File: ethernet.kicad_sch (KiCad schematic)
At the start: 58 parts, among them J8001 Bus_RJ45_5-2337992-8, U8001 KSZ9031RNXCA, Y8001 Oscillator_SMD_25MHz_KX-7

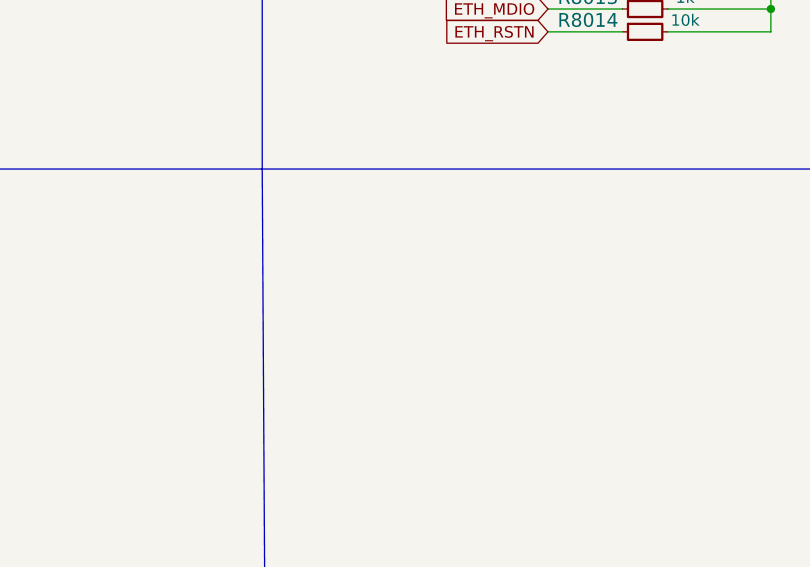
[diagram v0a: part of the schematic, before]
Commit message: Improve PCB after layout review
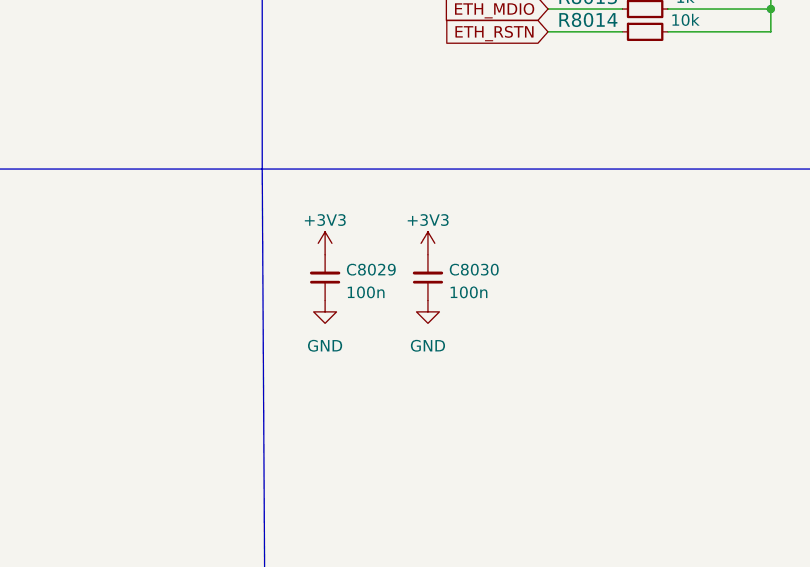
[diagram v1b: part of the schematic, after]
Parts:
- added C8029, C8030: C_100n_0402, antmicro-footprints:C_0402_1005Metric, symbol antmicroCapacitors0402:C_100n_0402
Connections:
- net +3V3: now also C8029.2, C8030.2
- net GND: now also C8029.1, C8030.1
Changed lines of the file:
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@@
     (pin "2")
+  )
+  (symbol (lib_id "sodimm-ddr5-tester:GND") (at 147.32 189.865 0) (unit 1)
+    (in_bom yes) (on_board yes) (fields_autoplaced)
+    (property "Reference" "#PWR0303" (id 0) (at 147.32 196.215 0)
+      (effects (font (size 1.27 1.27)) hide)
+    )
+    (property "Value" "GND" (id 1) (at 147.32 194.945 0))
+    (property "Footprint" "" (id 2) (at 147.32 189.865 0)
+      (effects (font (size 1.27 1.27)) hide)
+    )
+    (property "Datasheet" "" (id 3) (at 147.32 189.865 0)
+      (effects (font (size 1.27 1.27)) hide)
+    )
+    (property "Author" "Antmicro" (id 4) (at 156.21 197.485 0)
+      (effects (font (size 1.27 1.27) (thickness 0.15)) (justify left bottom) hide)
+    )
+    (property "License" "Apache-2.0" (id 5) (at 156.21 200.025 0)
+      (effects (font (size 1.27 1.27) (thickness 0.15)) (justify left bottom) hide)
+    )
+    (pin "1")
+  )
+  (symbol (lib_id "sodimm-ddr5-tester:+3V3") (at 158.75 184.785 0) (unit 1)
+    (in_bom yes) (on_board yes)
+    (property "Reference" "#PWR0305" (id 0) (at 158.75 188.595 0)
+      (effects (font (size 1.27 1.27)) hide)
+    )
+    (property "Value" "+3V3" (id 1) (at 158.75 180.975 0))
+    (property "Footprint" "" (id 2) (at 158.75 184.785 0)
+      (effects (font (size 1.27 1.27)) hide)
+    )
+    (property "Datasheet" "" (id 3) (at 158.75 184.785 0)
+      (effects (font (size 1.27 1.27)) hide)
+    )
+    (pin "1")
   )
   (symbol (lib_id "sodimm-ddr5-tester:GNDS") (at 78.74 244.475 0) (mirror y) (unit 1)
@@
     (pin "1")
   )
+  (symbol (lib_id "antmicroCapacitors0402:C_100n_0402") (at 158.75 189.865 90) (unit 1)
+    (in_bom yes) (on_board yes) (fields_autoplaced)
+    (property "Reference" "C8030" (id 0) (at 161.0741 186.488 90)
+      (effects (font (size 1.27 1.27) (thickness 0.15)) (justify right))
+    )
+    (property "Value" "C_100n_0402" (id 1) (at 168.91 169.545 0)
+      (effects (font (size 1.27 1.27) (thickness 0.15)) (justify left bottom) hide)
+    )
+    (property "Footprint" "antmicro-footprints:C_0402_1005Metric" (id 2) (at 171.45 169.545 0)
+      (effects (font (size 1.27 1.27) (thickness 0.15)) (justify left bottom) hide)
+    )
+    (property "Datasheet" "https://www.murata.com/products/productdetail?partno=GRM155R61H104KE14%23" (id 3) (at 173.99 169.545 0)
+      (effects (font (size 1.27 1.27) (thickness 0.15)) (justify left bottom) hide)
+    )
+    (property "MPN" "GRM155R61H104KE14D" (id 4) (at 176.53 169.545 0)
+      (effects (font (size 1.27 1.27) (thickness 0.15)) (justify left bottom) hide)
+    )
+    (property "Manufacturer" "Murata" (id 5) (at 179.07 169.545 0)
+      (effects (font (size 1.27 1.27) (thickness 0.15)) (justify left bottom) hide)
+    )
+    (property "License" "Apache-2.0" (id 6) (at 181.61 169.545 0)
+      (effects (font (size 1.27 1.27) (thickness 0.15)) (justify left bottom) hide)
+    )
+    (property "Author" "Antmicro" (id 7) (at 184.15 169.545 0)
+      (effects (font (size 1.27 1.27) (thickness 0.15)) (justify left bottom) hide)
+    )
+    (property "Val" "100n" (id 8) (at 161.0741 189.0117 90)
+      (effects (font (size 1.27 1.27) (thickness 0.15)) (justify right))
+    )
+    (property "Voltage" "50V" (id 9) (at 186.69 169.545 0)
+      (effects (font (size 1.27 1.27)) (justify left bottom) hide)
+    )
+    (property "Dielectric" "X5R" (id 10) (at 189.23 169.545 0)
+      (effects (font (size 1.27 1.27)) (justify left bottom) hide)
+    )
+    (pin "1")
+    (pin "2")
+  )
   (symbol (lib_id "antmicroFerriteBeadsandChips:FB_120Z_2A_Murata-BLM18PG_0603") (at 26.035 140.97 0) (unit 1)
     (in_bom yes) (on_board yes) (fields_autoplaced)
@@
     (pin "2")
   )
+  (symbol (lib_id "sodimm-ddr5-tester:+3V3") (at 147.32 184.785 0) (unit 1)
+    (in_bom yes) (on_board yes)
+    (property "Reference" "#PWR0302" (id 0) (at 147.32 188.595 0)
+      (effects (font (size 1.27 1.27)) hide)
+    )
+    (property "Value" "+3V3" (id 1) (at 147.32 180.975 0))
+    (property "Footprint" "" (id 2) (at 147.32 184.785 0)
+      (effects (font (size 1.27 1.27)) hide)
+    )
+    (property "Datasheet" "" (id 3) (at 147.32 184.785 0)
+      (effects (font (size 1.27 1.27)) hide)
+    )
+    (pin "1")
+  )
   (symbol (lib_id "sodimm-ddr5-tester:R_10k_0402") (at 180.34 147.32 0) (unit 1)
     (in_bom yes) (on_board yes)
@@
     (pin "1")
     (pin "2")
+  )
+  (symbol (lib_id "sodimm-ddr5-tester:GND") (at 158.75 189.865 0) (unit 1)
+    (in_bom yes) (on_board yes) (fields_autoplaced)
+    (property "Reference" "#PWR0304" (id 0) (at 158.75 196.215 0)
+      (effects (font (size 1.27 1.27)) hide)
+    )
+    (property "Value" "GND" (id 1) (at 158.75 194.945 0))
+    (property "Footprint" "" (id 2) (at 158.75 189.865 0)
+      (effects (font (size 1.27 1.27)) hide)
+    )
+    (property "Datasheet" "" (id 3) (at 158.75 189.865 0)
+      (effects (font (size 1.27 1.27)) hide)
+    )
+    (property "Author" "Antmicro" (id 4) (at 167.64 197.485 0)
+      (effects (font (size 1.27 1.27) (thickness 0.15)) (justify left bottom) hide)
+    )
+    (property "License" "Apache-2.0" (id 5) (at 167.64 200.025 0)
+      (effects (font (size 1.27 1.27) (thickness 0.15)) (justify left bottom) hide)
+    )
+    (pin "1")
   )
   (symbol (lib_id "sodimm-ddr5-tester:R_10k_0402") (at 180.34 152.4 0) (unit 1)
@@
     (pin "9")
   )
+  (symbol (lib_id "antmicroCapacitors0402:C_100n_0402") (at 147.32 189.865 90) (unit 1)
+    (in_bom yes) (on_board yes) (fields_autoplaced)
+    (property "Reference" "C8029" (id 0) (at 149.6441 186.488 90)
+      (effects (font (size 1.27 1.27) (thickness 0.15)) (justify right))
+    )
+    (property "Value" "C_100n_0402" (id 1) (at 157.48 169.545 0)
+      (effects (font (size 1.27 1.27) (thickness 0.15)) (justify left bottom) hide)
+    )
+    (property "Footprint" "antmicro-footprints:C_0402_1005Metric" (id 2) (at 160.02 169.545 0)
+      (effects (font (size 1.27 1.27) (thickness 0.15)) (justify left bottom) hide)
+    )
+    (property "Datasheet" "https://www.murata.com/products/productdetail?partno=GRM155R61H104KE14%23" (id 3) (at 162.56 169.545 0)
+      (effects (font (size 1.27 1.27) (thickness 0.15)) (justify left bottom) hide)
+    )
+    (property "MPN" "GRM155R61H104KE14D" (id 4) (at 165.1 169.545 0)
+      (effects (font (size 1.27 1.27) (thickness 0.15)) (justify left bottom) hide)
+    )
+    (property "Manufacturer" "Murata" (id 5) (at 167.64 169.545 0)
+      (effects (font (size 1.27 1.27) (thickness 0.15)) (justify left bottom) hide)
+    )
+    (property "License" "Apache-2.0" (id 6) (at 170.18 169.545 0)
+      (effects (font (size 1.27 1.27) (thickness 0.15)) (justify left bottom) hide)
+    )
+    (property "Author" "Antmicro" (id 7) (at 172.72 169.545 0)
+      (effects (font (size 1.27 1.27) (thickness 0.15)) (justify left bottom) hide)
+    )
+    (property "Val" "100n" (id 8) (at 149.6441 189.0117 90)
+      (effects (font (size 1.27 1.27) (thickness 0.15)) (justify right))
+    )
+    (property "Voltage" "50V" (id 9) (at 175.26 169.545 0)
+      (effects (font (size 1.27 1.27)) (justify left bottom) hide)
+    )
+    (property "Dielectric" "X5R" (id 10) (at 177.8 169.545 0)
+      (effects (font (size 1.27 1.27)) (justify left bottom) hide)
+    )
+    (pin "1")
+    (pin "2")
+  )
   (symbol (lib_id "sodimm-ddr5-tester:R_10k_0402") (at 180.34 149.86 0) (unit 1)

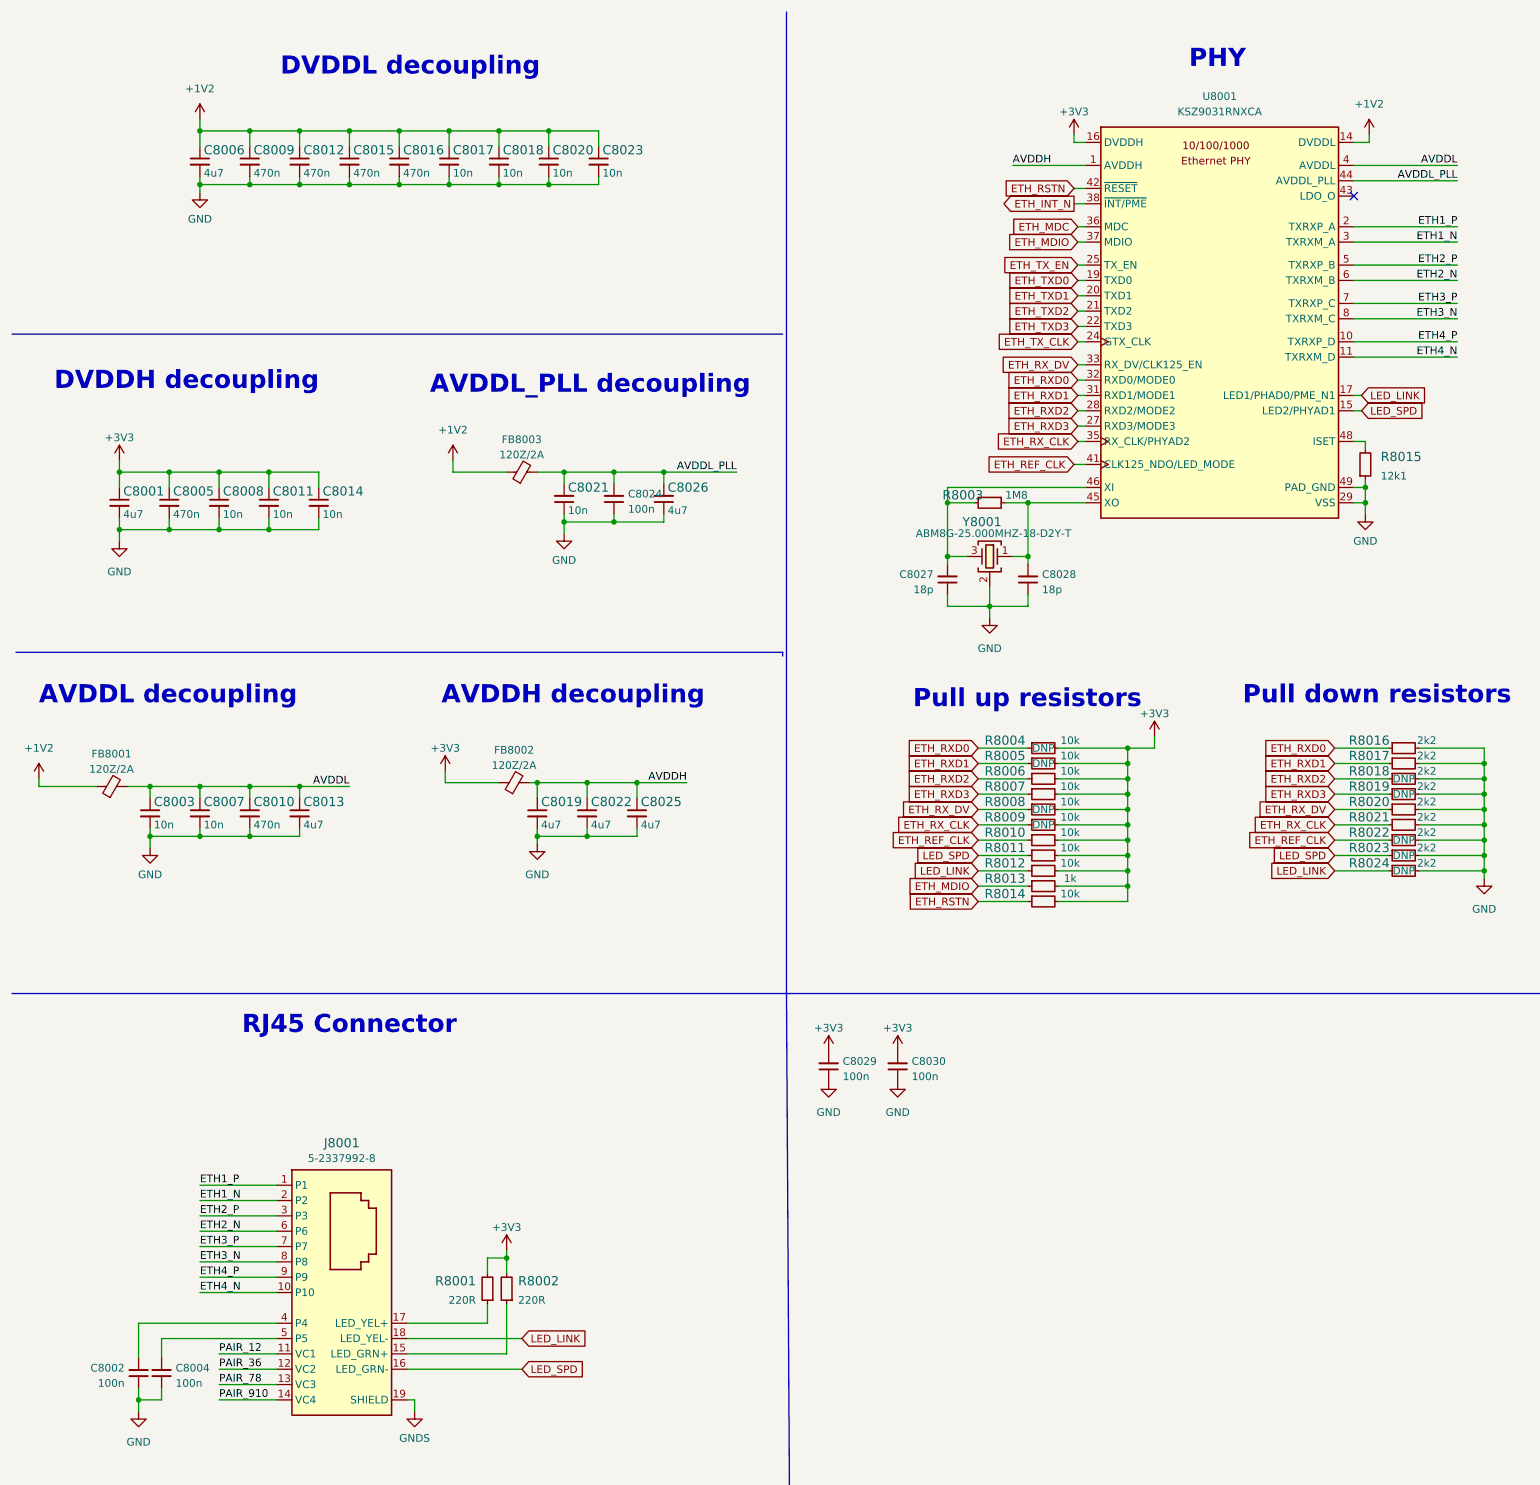
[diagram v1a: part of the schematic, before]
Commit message: Re-annotate schematic
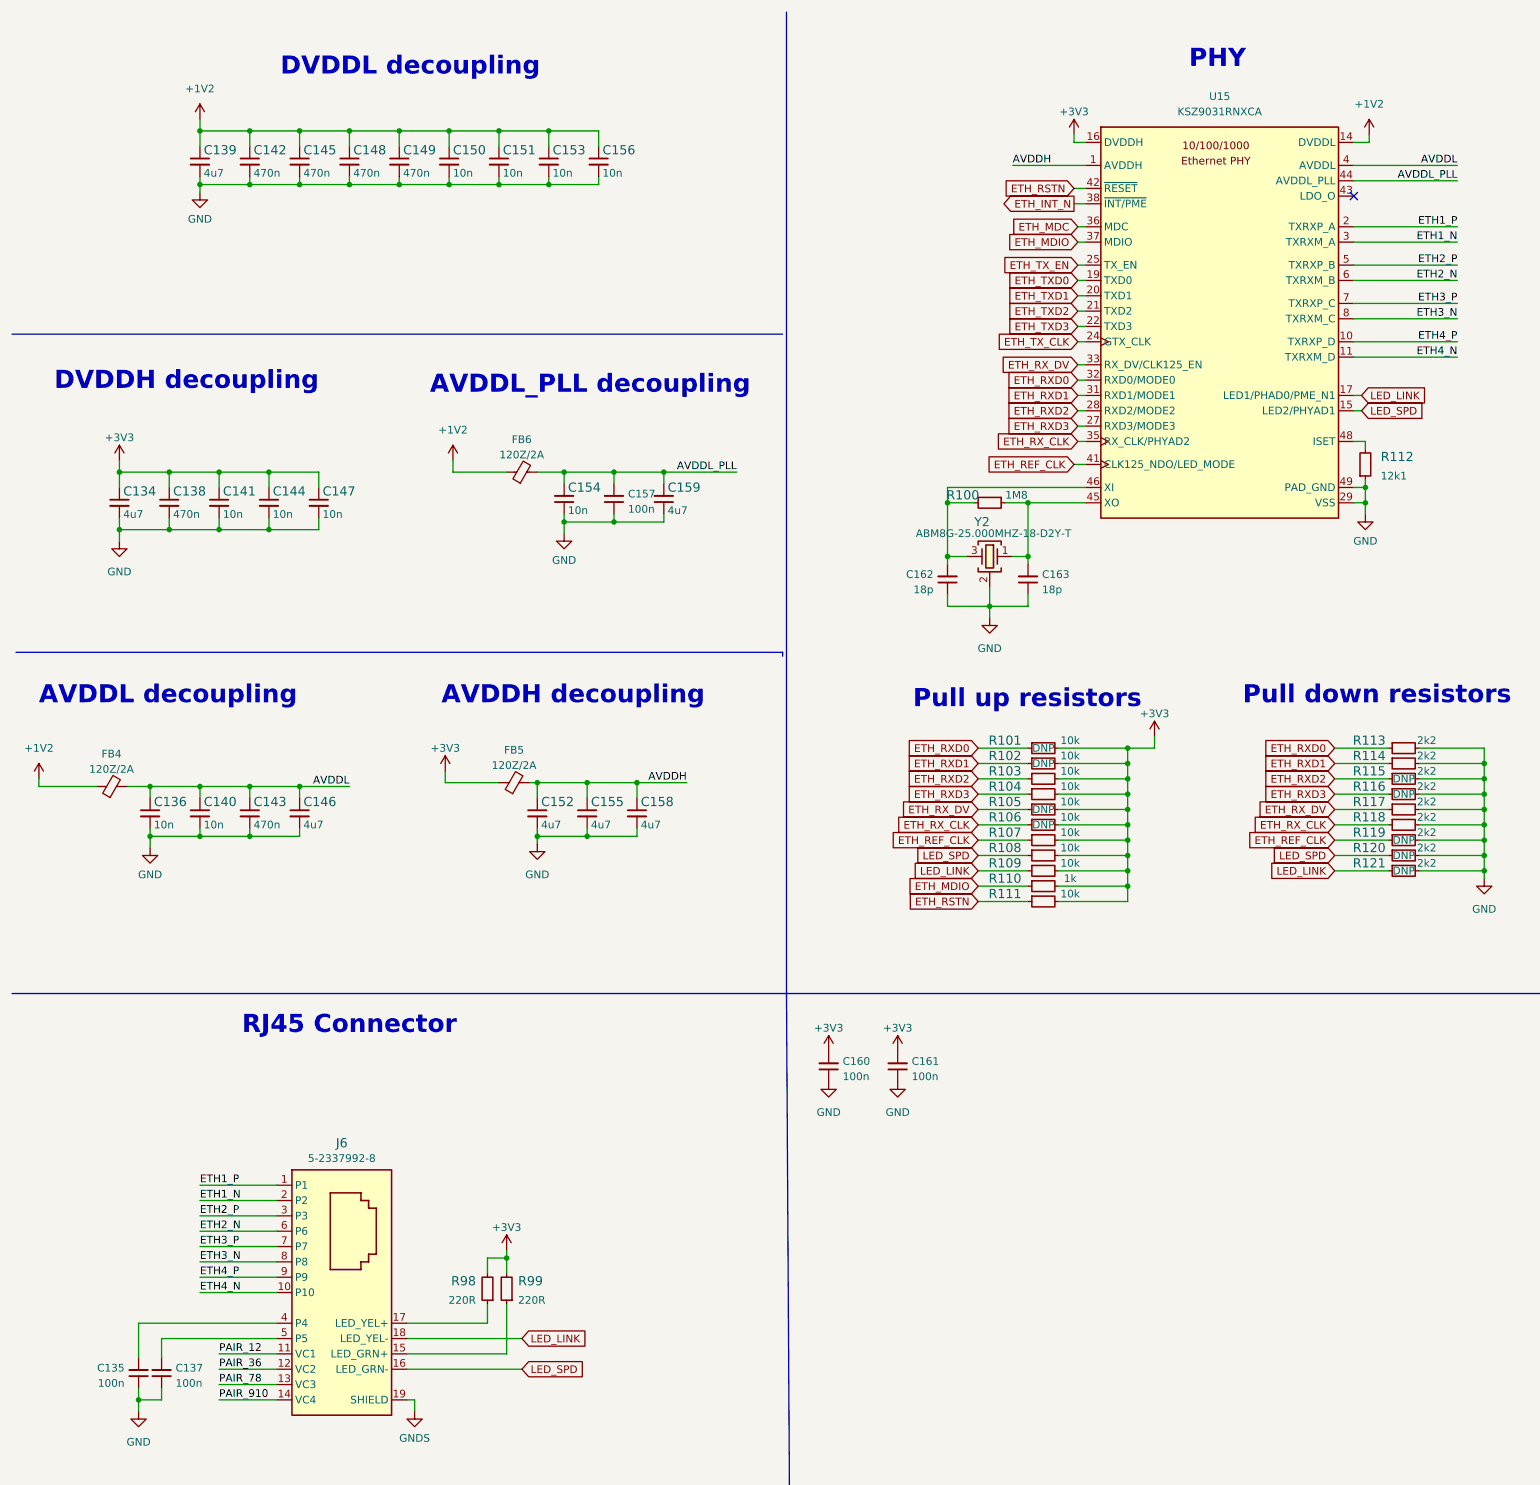
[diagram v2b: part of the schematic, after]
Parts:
- renumbered C8001 to C134, C8002 to C135, C8003 to C136, C8004 to C137, C8005 to C138, C8006 to C139, C8007 to C140, C8008 to C141, C8009 to C142, C8010 to C143, C8011 to C144, C8012 to C145, C8013 to C146, C8014 to C147, C8015 to C148, C8016 to C149, C8017 to C150, C8018 to C151, C8019 to C152, C8020 to C153, C8021 to C154, C8022 to C155, C8023 to C156, C8024 to C157, C8025 to C158, C8026 to C159, C8029 to C160, C8030 to C161, C8027 to C162, C8028 to C163, FB8001 to FB4, FB8002 to FB5, FB8003 to FB6, J8001 to J6, R8003 to R100, R8004 to R101, R8005 to R102, R8006 to R103, R8007 to R104, R8008 to R105, R8009 to R106, R8010 to R107, R8011 to R108, R8012 to R109, R8013 to R110, R8014 to R111, R8015 to R112, R8016 to R113, R8017 to R114, R8018 to R115, R8019 to R116, R8020 to R117, R8021 to R118, R8022 to R119, R8023 to R120, R8024 to R121, R8001 to R98, R8002 to R99, U8001 to U15, Y8001 to Y2

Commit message: Add local libraries
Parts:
- C135, C137, C157, C160, C161: footprint antmicro-footprints:C_0402_1005Metric -> sodimm-ddr5-tester-footprints:C_0402_1005Metric; symbol antmicroCapacitors0402:C_100n_0402 -> sodimm-ddr5-tester:C_100n_0402
- C162, C163: footprint antmicro-footprints:C_0402_1005Metric -> sodimm-ddr5-tester-footprints:C_0402_1005Metric; symbol antmicroCapacitors0402:C_18p_0402 -> sodimm-ddr5-tester:C_18p_0402
- FB4, FB5, FB6: footprint antmicro-footprints:FB_0603_1608Metric -> sodimm-ddr5-tester-footprints:FB_0603_1608Metric; symbol antmicroFerriteBeadsandChips:FB_120Z_2A_Murata-BLM18PG_0603 -> sodimm-ddr5-tester:FB_120Z_2A_Murata-BLM18PG_0603

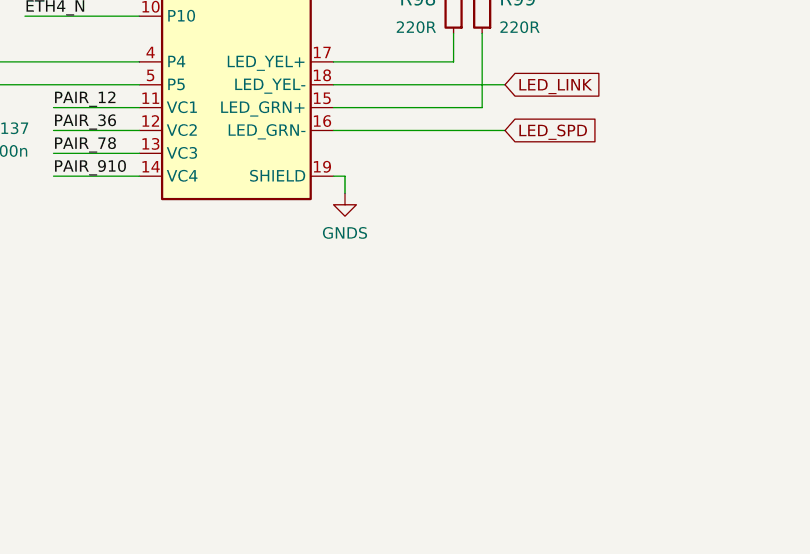
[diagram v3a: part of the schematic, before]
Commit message: Change via drill size. Replace the holes for mounting the PCIe backplate with plated ones. Move PCB SHA marking. Increase clearance to 12V planes and traces
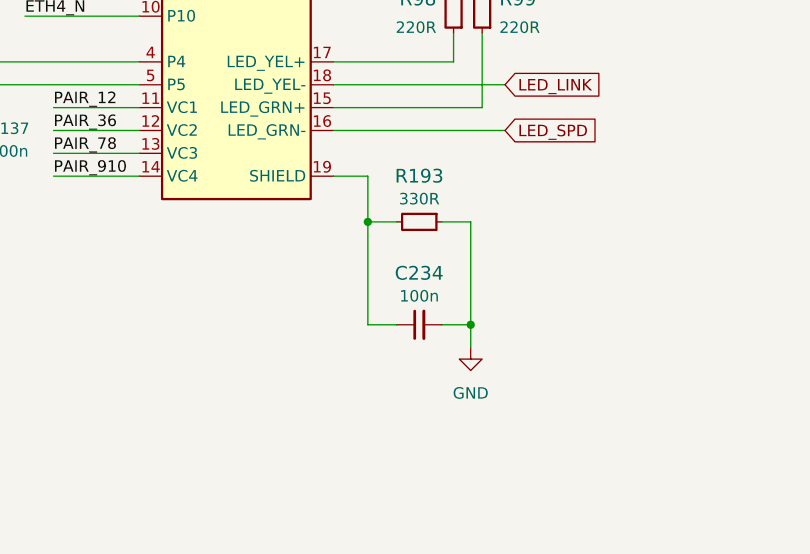
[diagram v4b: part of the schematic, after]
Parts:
- added C234: C_100n_0402, sodimm-ddr5-tester-footprints:C_0402_1005Metric, symbol sodimm-ddr5-tester:C_100n_0402
- added R193: R_330R_0402, sodimm-ddr5-tester-footprints:R_0402_1005Metric, symbol sodimm-ddr5-tester:R_330R_0402
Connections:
- net GND: now also C234.2, R193.1
- net GNDS: no longer names the net of J6.19 (SHIELD), J6.20 (SHIELD)
- net GNDS: now also C234.1, R193.2
